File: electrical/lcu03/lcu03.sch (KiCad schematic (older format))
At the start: 93 parts, among them P1 screw, P10 swd, P11 stepper_conn, P12 stepper_conn, P13 stepper_conn, P2 screw, P3 screw, P4 screw, P5 ext-1, P6 ~rst~, P7 mode, P8 ext-2, P9 USB_B, Q1 bc857, Q2 bv847, Q3 bc857, Q4 ntd18n06l, U1 crystal-4pin, U2 CP2102, U3 m24c02, U4 NCP3063, U5 MCP1703T-3302E/CB, U6 ts881, U7 lb1930mc

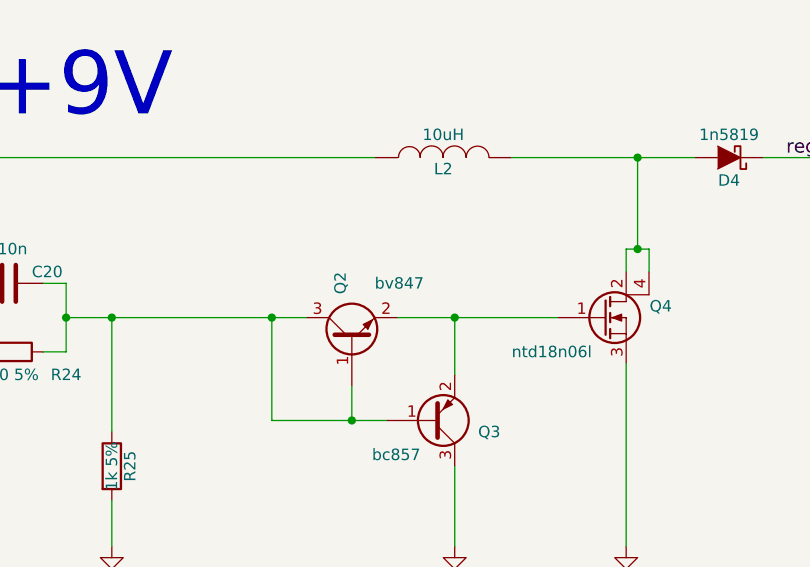
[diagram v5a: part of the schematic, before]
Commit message: Looks like done with assigning footprints.
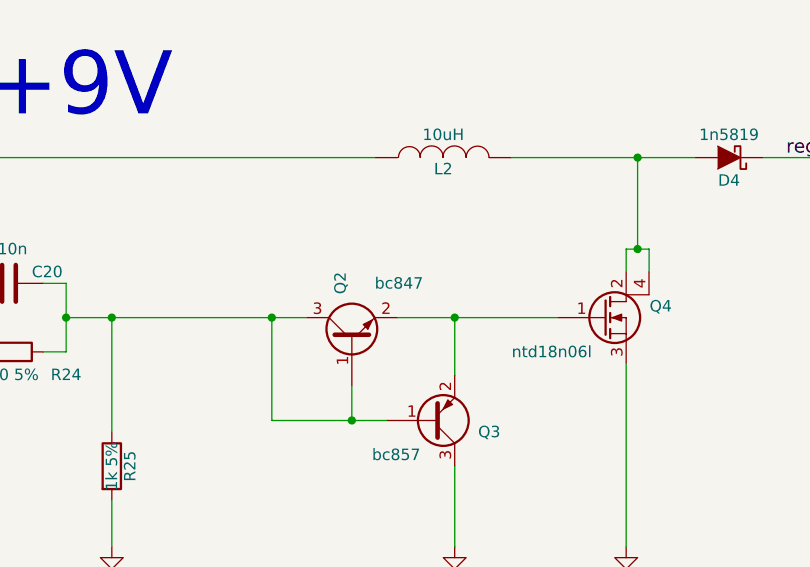
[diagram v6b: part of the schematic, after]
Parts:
- C1, C10, C11, C12, C13, C14, C15, C16, C18, C19, C2, C20, C21, C23, C24, C3, C4, C5, C6, C7, C8, C9: footprint Capacitors_SMD:C_0805_HandSoldering -> Capacitors_SMD:C_0805
- P10: footprint Socket_Strips:Socket_Strip_Straight_1x03 -> Pin_Headers:Pin_Header_Straight_1x03
- P6: footprint Pin_Headers:Pin_Header_Straight_1x01 -> Measurement_Points:Measurement_Point_Round-TH_Small
- P7: footprint Pin_Headers:Pin_Header_Angled_1x02 -> Pin_Headers:Pin_Header_Straight_1x02
- P8: footprint Pin_Headers:Pin_Header_Angled_1x08 -> Pin_Headers:Pin_Header_Straight_1x08
- Q2: value bv847 -> bc847
- Q4: footprint (none) -> my-lib:my-DPAK
- R1, R2, R3, R4, R5, R6, R7, R8: footprint Resistors_SMD:R_0805_HandSoldering -> Resistors_SMD:R_0805
- U7: footprint (none) -> my-lib:lb1930mc
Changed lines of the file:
@@
 F 0 "R8" V 4280 3300 50  0000 C CNN
 F 1 "10k 5%" V 4100 3300 50  0000 C CNN
-F 2 "Resistors_SMD:R_0805_HandSoldering" V 4130 3300 30  0001 C CNN
+F 2 "Resistors_SMD:R_0805" V 4130 3300 30  0001 C CNN
 F 3 "" H 4200 3300 30  0000 C CNN
 	1    4200 3300
@@
 F 0 "C4" H 4225 3800 50  0000 L CNN
 F 1 "100n" H 4225 3600 50  0000 L CNN
-F 2 "Capacitors_SMD:C_0805_HandSoldering" H 4238 3550 30  0001 C CNN
+F 2 "Capacitors_SMD:C_0805" H 4238 3550 30  0001 C CNN
 F 3 "" H 4200 3700 60  0000 C CNN
 	1    4200 3700
@@
 F 0 "C2" H 1675 4150 50  0000 L CNN
 F 1 "18p" H 1675 3950 50  0000 L CNN
-F 2 "Capacitors_SMD:C_0805_HandSoldering" H 1688 3900 30  0001 C CNN
+F 2 "Capacitors_SMD:C_0805" H 1688 3900 30  0001 C CNN
 F 3 "" H 1650 4050 60  0000 C CNN
 	1    1650 4050
@@
 F 0 "C3" H 3375 5350 50  0000 L CNN
 F 1 "18p" H 3375 5150 50  0000 L CNN
-F 2 "Capacitors_SMD:C_0805_HandSoldering" H 3388 5100 30  0001 C CNN
+F 2 "Capacitors_SMD:C_0805" H 3388 5100 30  0001 C CNN
 F 3 "" H 3350 5250 60  0000 C CNN
 	1    3350 5250
@@
 F 0 "R6" V 3830 5000 50  0000 C CNN
 F 1 "100 5%" V 3650 5000 50  0000 C CNN
-F 2 "Resistors_SMD:R_0805_HandSoldering" V 3680 5000 30  0001 C CNN
+F 2 "Resistors_SMD:R_0805" V 3680 5000 30  0001 C CNN
 F 3 "" H 3750 5000 30  0000 C CNN
 	1    3750 5000
@@
 F 0 "R5" V 3780 7950 50  0000 C CNN
 F 1 "10k 5%" V 3700 7950 50  0000 C CNN
-F 2 "Resistors_SMD:R_0805_HandSoldering" V 3630 7950 30  0001 C CNN
+F 2 "Resistors_SMD:R_0805" V 3630 7950 30  0001 C CNN
 F 3 "" H 3700 7950 30  0000 C CNN
 	1    3700 7950
@@
 F 0 "C21" H 16075 17650 50  0000 L CNN
 F 1 "4u7" H 16075 17450 50  0000 L CNN
-F 2 "Capacitors_SMD:C_0805_HandSoldering" H 16088 17400 30  0001 C CNN
+F 2 "Capacitors_SMD:C_0805" H 16088 17400 30  0001 C CNN
 F 3 "" H 16050 17550 60  0000 C CNN
 	1    16050 17550
@@
 F 0 "C18" H 14575 17650 50  0000 L CNN
 F 1 "4u7" H 14575 17450 50  0000 L CNN
-F 2 "Capacitors_SMD:C_0805_HandSoldering" H 14588 17400 30  0001 C CNN
+F 2 "Capacitors_SMD:C_0805" H 14588 17400 30  0001 C CNN
 F 3 "" H 14550 17550 60  0000 C CNN
 	1    14550 17550
@@
 F 0 "C1" H 775 19500 50  0000 L CNN
 F 1 "100n" H 775 19300 50  0000 L CNN
-F 2 "Capacitors_SMD:C_0805_HandSoldering" H 788 19250 30  0001 C CNN
+F 2 "Capacitors_SMD:C_0805" H 788 19250 30  0001 C CNN
 F 3 "" H 750 19400 60  0000 C CNN
 	1    750  19400
@@
 F 0 "R1" V 830 18700 50  0000 C CNN
 F 1 "10k 5%" V 650 18700 50  0000 C CNN
-F 2 "Resistors_SMD:R_0805_HandSoldering" V 680 18700 30  0001 C CNN
+F 2 "Resistors_SMD:R_0805" V 680 18700 30  0001 C CNN
 F 3 "" H 750 18700 30  0000 C CNN
 	1    750  18700
@@
 F 0 "C5" H 5575 19550 50  0000 L CNN
 F 1 "100n" H 5575 19350 50  0000 L CNN
-F 2 "Capacitors_SMD:C_0805_HandSoldering" H 5588 19300 30  0001 C CNN
+F 2 "Capacitors_SMD:C_0805" H 5588 19300 30  0001 C CNN
 F 3 "" H 5550 19450 60  0000 C CNN
 	1    5550 19450
@@
 F 0 "C6" H 5925 19550 50  0000 L CNN
 F 1 "4u7" H 5925 19350 50  0000 L CNN
-F 2 "Capacitors_SMD:C_0805_HandSoldering" H 5938 19300 30  0001 C CNN
+F 2 "Capacitors_SMD:C_0805" H 5938 19300 30  0001 C CNN
 F 3 "" H 5900 19450 60  0000 C CNN
 	1    5900 19450
@@
 F 0 "C15" H 12625 20650 50  0000 L CNN
 F 1 "100n" H 12625 20450 50  0000 L CNN
-F 2 "Capacitors_SMD:C_0805_HandSoldering" H 12638 20400 30  0001 C CNN
+F 2 "Capacitors_SMD:C_0805" H 12638 20400 30  0001 C CNN
 F 3 "" H 12600 20550 60  0000 C CNN
 	1    12600 20550
@@
 F 0 "C19" H 14975 20600 50  0000 L CNN
 F 1 "1n2" H 14975 20400 50  0000 L CNN
-F 2 "Capacitors_SMD:C_0805_HandSoldering" H 14988 20350 30  0001 C CNN
+F 2 "Capacitors_SMD:C_0805" H 14988 20350 30  0001 C CNN
 F 3 "" H 14950 20500 60  0000 C CNN
 	1    14950 20500
@@
 F 0 "C24" H 19225 20050 50  0000 L CNN
 F 1 "100n" H 19225 19850 50  0000 L CNN
-F 2 "Capacitors_SMD:C_0805_HandSoldering" H 19238 19800 30  0001 C CNN
+F 2 "Capacitors_SMD:C_0805" H 19238 19800 30  0001 C CNN
 F 3 "" H 19200 19950 60  0000 C CNN
 	1    19200 19950
@@
 F 0 "R2" V 1280 12600 50  0000 C CNN
 F 1 "1k 5%" V 1200 12600 50  0000 C CNN
-F 2 "Resistors_SMD:R_0805_HandSoldering" V 1130 12600 30  0001 C CNN
+F 2 "Resistors_SMD:R_0805" V 1130 12600 30  0001 C CNN
 F 3 "" H 1200 12600 30  0000 C CNN
 	1    1200 12600
@@
 F 0 "R3" V 1780 12600 50  0000 C CNN
 F 1 "1k 5%" V 1700 12600 50  0000 C CNN
-F 2 "Resistors_SMD:R_0805_HandSoldering" V 1630 12600 30  0001 C CNN
+F 2 "Resistors_SMD:R_0805" V 1630 12600 30  0001 C CNN
 F 3 "" H 1700 12600 30  0000 C CNN
 	1    1700 12600
@@
 F 0 "P7" H 3300 7300 50  0000 C CNN
 F 1 "mode" V 3400 7150 50  0000 C CNN
-F 2 "Pin_Headers:Pin_Header_Angled_1x02" H 3300 7150 60  0001 C CNN
+F 2 "Pin_Headers:Pin_Header_Straight_1x02" H 3300 7150 60  0001 C CNN
 F 3 "" H 3300 7150 60  0000 C CNN
 	1    3300 7150
@@
 F 0 "P10" H 10550 5900 50  0000 C CNN
 F 1 "swd" V 10650 5700 50  0000 C CNN
-F 2 "Socket_Strips:Socket_Strip_Straight_1x03" H 10550 5700 60  0001 C CNN
+F 2 "Pin_Headers:Pin_Header_Straight_1x03" H 10550 5700 60  0001 C CNN
 F 3 "" H 10550 5700 60  0000 C CNN
 	1    10550 5700
@@
 F 0 "P6" H 3250 3600 50  0000 C CNN
 F 1 "~rst~" V 3350 3500 50  0000 C CNN
-F 2 "Pin_Headers:Pin_Header_Straight_1x01" H 3250 3500 60  0001 C CNN
+F 2 "Measurement_Points:Measurement_Point_Round-TH_Small" H 3250 3500 60  0001 C CNN
 F 3 "" H 3250 3500 60  0000 C CNN
 	1    3250 3500
@@
 F 0 "R4" V 3630 12350 50  0000 C CNN
 F 1 "10k 5%" V 3550 12350 50  0000 C CNN
-F 2 "Resistors_SMD:R_0805_HandSoldering" V 3480 12350 30  0001 C CNN
+F 2 "Resistors_SMD:R_0805" V 3480 12350 30  0001 C CNN
 F 3 "" H 3550 12350 30  0000 C CNN
 	1    3550 12350
@@
 F 0 "C8" H 10625 1350 50  0000 L CNN
 F 1 "100n" H 10625 1150 50  0000 L CNN
-F 2 "Capacitors_SMD:C_0805_HandSoldering" H 10638 1100 30  0001 C CNN
+F 2 "Capacitors_SMD:C_0805" H 10638 1100 30  0001 C CNN
 F 3 "" H 10600 1250 60  0000 C CNN
 	1    10600 1250
@@
 F 0 "C9" H 10925 1350 50  0000 L CNN
 F 1 "100n" H 10925 1150 50  0000 L CNN
-F 2 "Capacitors_SMD:C_0805_HandSoldering" H 10938 1100 30  0001 C CNN
+F 2 "Capacitors_SMD:C_0805" H 10938 1100 30  0001 C CNN
 F 3 "" H 10900 1250 60  0000 C CNN
 	1    10900 1250
@@
 F 0 "C10" H 11225 1350 50  0000 L CNN
 F 1 "100n" H 11225 1150 50  0000 L CNN
-F 2 "Capacitors_SMD:C_0805_HandSoldering" H 11238 1100 30  0001 C CNN
+F 2 "Capacitors_SMD:C_0805" H 11238 1100 30  0001 C CNN
 F 3 "" H 11200 1250 60  0000 C CNN
 	1    11200 1250
@@
 F 0 "C11" H 11525 1350 50  0000 L CNN
 F 1 "100n" H 11525 1150 50  0000 L CNN
-F 2 "Capacitors_SMD:C_0805_HandSoldering" H 11538 1100 30  0001 C CNN
+F 2 "Capacitors_SMD:C_0805" H 11538 1100 30  0001 C CNN
 F 3 "" H 11500 1250 60  0000 C CNN
 	1    11500 1250
@@
 F 0 "C12" H 11825 1350 50  0000 L CNN
 F 1 "4u7" H 11825 1150 50  0000 L CNN
-F 2 "Capacitors_SMD:C_0805_HandSoldering" H 11838 1100 30  0001 C CNN
+F 2 "Capacitors_SMD:C_0805" H 11838 1100 30  0001 C CNN
 F 3 "" H 11800 1250 60  0000 C CNN
 	1    11800 1250
@@
 F 0 "R7" V 4230 7950 50  0000 C CNN
 F 1 "10k 5%" V 4150 7950 50  0000 C CNN
-F 2 "Resistors_SMD:R_0805_HandSoldering" V 4080 7950 30  0001 C CNN
+F 2 "Resistors_SMD:R_0805" V 4080 7950 30  0001 C CNN
 F 3 "" H 4150 7950 30  0000 C CNN
 	1    4150 7950
@@
 F 0 "C16" H 13775 20950 50  0000 L CNN
 F 1 "10n" H 13775 20750 50  0000 L CNN
-F 2 "Capacitors_SMD:C_0805_HandSoldering" H 13788 20700 30  0001 C CNN
+F 2 "Capacitors_SMD:C_0805" H 13788 20700 30  0001 C CNN
 F 3 "" H 13750 20850 60  0000 C CNN
 	1    13750 20850
@@
 F 0 "C13" H 12325 20650 50  0000 L CNN
 F 1 "4u7" H 12325 20450 50  0000 L CNN
-F 2 "Capacitors_SMD:C_0805_HandSoldering" H 12338 20400 30  0001 C CNN
+F 2 "Capacitors_SMD:C_0805" H 12338 20400 30  0001 C CNN
 F 3 "" H 12300 20550 60  0000 C CNN
 	1    12300 20550
@@
 F 0 "C20" V 15450 20050 50  0000 L CNN
 F 1 "10n" V 15350 19900 50  0000 L CNN
-F 2 "Capacitors_SMD:C_0805_HandSoldering" H 15538 19800 30  0001 C CNN
+F 2 "Capacitors_SMD:C_0805" H 15538 19800 30  0001 C CNN
 F 3 "" H 15500 19950 60  0000 C CNN
 	1    15500 19950
@@
 P 17000 20200
 F 0 "Q2" H 17300 20250 50  0000 R CNN
-F 1 "bv847" V 17250 20100 50  0000 R CNN
+F 1 "bc847" V 17250 20100 50  0000 R CNN
 F 2 "TO_SOT_Packages_SMD:SOT-23_Handsoldering" H 17200 20300 50  0001 C CNN
 F 3 "" H 17000 20200 50  0000 C CNN
@@
 F 0 "Q4" H 18400 20150 50  0000 R CNN
 F 1 "ntd18n06l" H 18050 19950 50  0000 R CNN
-F 2 "" H 18300 20200 50  0001 C CNN
+F 2 "my-lib:my-DPAK" H 18300 20200 50  0001 C CNN
 F 3 "" H 18100 20100 50  0000 C CNN
 	1    18100 20100
@@
 F 0 "U7" H 21600 1400 60  0000 C CNN
 F 1 "lb1930mc" H 21600 2400 60  0000 C CNN
-F 2 "" H 21600 1900 60  0001 C CNN
+F 2 "my-lib:lb1930mc" H 21600 1900 60  0001 C CNN
 F 3 "" H 21600 1900 60  0000 C CNN
 	1    21600 1900
@@
 F 0 "C14" H 12375 12200 50  0000 L CNN
 F 1 "100n" H 12375 12000 50  0000 L CNN
-F 2 "Capacitors_SMD:C_0805_HandSoldering" H 12388 11950 50  0001 C CNN
+F 2 "Capacitors_SMD:C_0805" H 12388 11950 50  0001 C CNN
 F 3 "" H 12350 12100 50  0000 C CNN
 	1    12350 12100
@@
 F 0 "C7" H 6075 22100 50  0000 L CNN
 F 1 "4u7" H 6075 21900 50  0000 L CNN
-F 2 "Capacitors_SMD:C_0805_HandSoldering" H 6088 21850 30  0001 C CNN
+F 2 "Capacitors_SMD:C_0805" H 6088 21850 30  0001 C CNN
 F 3 "" H 6050 22000 60  0000 C CNN
 	1    6050 22000
@@
 F 0 "C23" H 17825 9050 50  0000 L CNN
 F 1 "100n" H 17825 8850 50  0000 L CNN
-F 2 "Capacitors_SMD:C_0805_HandSoldering" H 17838 8800 50  0001 C CNN
+F 2 "Capacitors_SMD:C_0805" H 17838 8800 50  0001 C CNN
 F 3 "" H 17800 8950 50  0000 C CNN
 	1    17800 8950
@@
 F 0 "P8" H 4550 13350 50  0000 C CNN
 F 1 "ext-2" V 4650 12900 50  0000 C CNN
-F 2 "Pin_Headers:Pin_Header_Angled_1x08" H 4550 12900 50  0001 C CNN
+F 2 "Pin_Headers:Pin_Header_Straight_1x08" H 4550 12900 50  0001 C CNN
 F 3 "" H 4550 12900 50  0000 C CNN
 	1    4550 12900

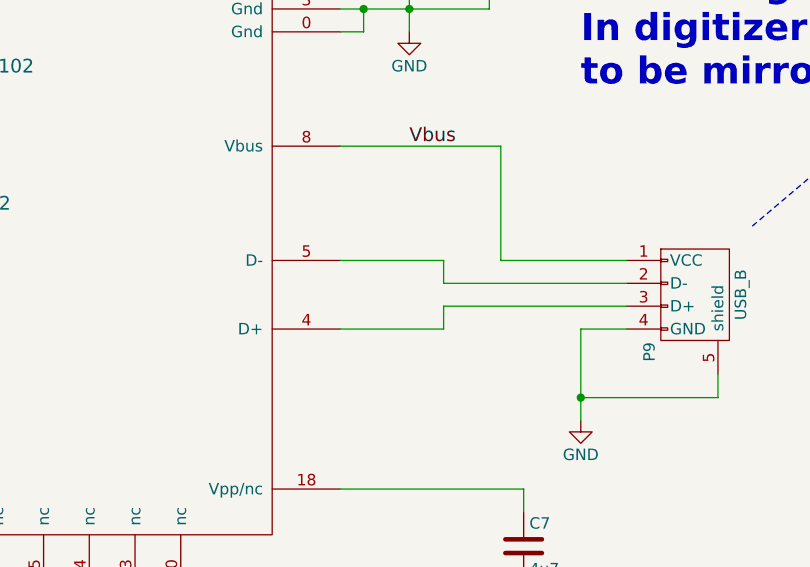
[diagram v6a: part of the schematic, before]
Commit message: Started placing components.
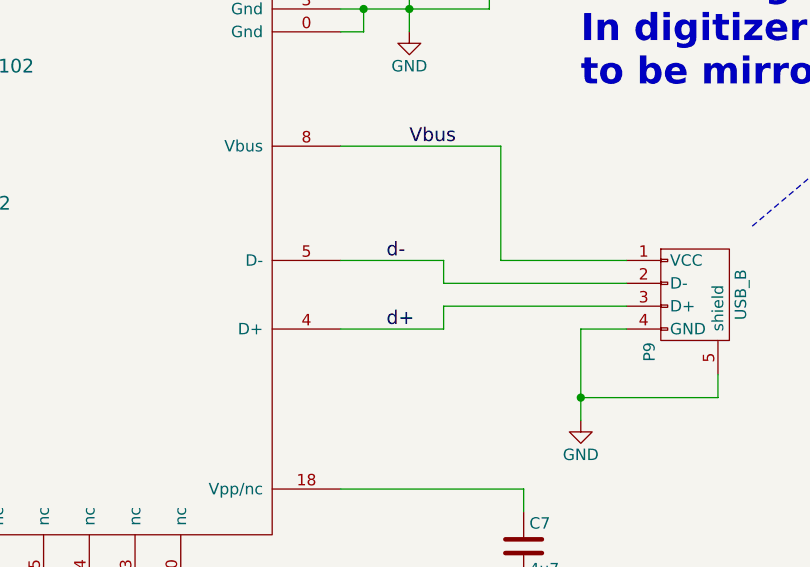
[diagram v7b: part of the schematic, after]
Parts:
- P11, P12, P13: footprint Connectors_JST_PH:Connectors_JST_B4B-PH-SM4-TB -> my-lib:JST_B4B-PH-SM4-TB
- P5: footprint Pin_Headers:Pin_Header_Angled_1x08 -> Pin_Headers:Pin_Header_Straight_1x08
- Q1, Q2, Q3, U5: footprint TO_SOT_Packages_SMD:SOT-23_Handsoldering -> TO_SOT_Packages_SMD:SOT-23
- U1: footprint crystal-smd-5x3:CRYSTAL-SMD-5x3 -> my-lib:CRYSTAL-SMD-5x3
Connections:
- net labels added: d+, d-
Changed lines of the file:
@@
 F 0 "U1" H 2550 4350 60  0000 C CNN
 F 1 "crystal-4pin" H 2550 5000 60  0000 C CNN
-F 2 "crystal-smd-5x3:CRYSTAL-SMD-5x3" H 2500 4650 60  0001 C CNN
+F 2 "my-lib:CRYSTAL-SMD-5x3" H 2500 4650 60  0001 C CNN
 F 3 "" H 2500 4650 60  0000 C CNN
 	1    2550 4650
@@
 F 0 "U5" H 15300 17250 60  0000 C CNN
 F 1 "MCP1703T-3302E/CB" H 15300 17600 60  0000 C CNN
-F 2 "TO_SOT_Packages_SMD:SOT-23_Handsoldering" H 15300 17300 60  0001 C CNN
+F 2 "TO_SOT_Packages_SMD:SOT-23" H 15300 17300 60  0001 C CNN
 F 3 "" H 15300 17300 60  0000 C CNN
 	1    15300 17300
@@
 F 0 "Q2" H 17300 20250 50  0000 R CNN
 F 1 "bc847" V 17250 20100 50  0000 R CNN
-F 2 "TO_SOT_Packages_SMD:SOT-23_Handsoldering" H 17200 20300 50  0001 C CNN
+F 2 "TO_SOT_Packages_SMD:SOT-23" H 17200 20300 50  0001 C CNN
 F 3 "" H 17000 20200 50  0000 C CNN
 	1    17000 20200
@@
 F 0 "Q3" H 17650 20600 50  0000 R CNN
 F 1 "bc857" H 17300 20700 50  0000 R CNN
-F 2 "TO_SOT_Packages_SMD:SOT-23_Handsoldering" H 17550 20650 50  0001 C CNN
+F 2 "TO_SOT_Packages_SMD:SOT-23" H 17550 20650 50  0001 C CNN
 F 3 "" H 17350 20550 50  0000 C CNN
 	1    17350 20550
@@
 F 0 "Q1" H 15700 5000 50  0000 R CNN
 F 1 "bc857" H 15350 5100 50  0000 R CNN
-F 2 "TO_SOT_Packages_SMD:SOT-23_Handsoldering" H 15600 5050 50  0001 C CNN
+F 2 "TO_SOT_Packages_SMD:SOT-23" H 15600 5050 50  0001 C CNN
 F 3 "" H 15400 4950 50  0000 C CNN
 	1    15400 4950
@@
 F 0 "P11" H 24900 2150 50  0000 C CNN
 F 1 "stepper_conn" V 24950 1800 50  0000 C CNN
-F 2 "Connectors_JST_PH:Connectors_JST_B4B-PH-SM4-TB" H 24850 1900 50  0001 C CNN
+F 2 "my-lib:JST_B4B-PH-SM4-TB" H 24850 1900 50  0001 C CNN
 F 3 "" H 24850 1900 50  0000 C CNN
 	1    24850 1900
@@
 F 0 "P12" H 28350 5400 50  0000 C CNN
 F 1 "stepper_conn" V 28400 5050 50  0000 C CNN
-F 2 "Connectors_JST_PH:Connectors_JST_B4B-PH-SM4-TB" H 28300 5150 50  0001 C CNN
+F 2 "my-lib:JST_B4B-PH-SM4-TB" H 28300 5150 50  0001 C CNN
 F 3 "" H 28300 5150 50  0000 C CNN
 	1    28300 5150
@@
 F 0 "P13" H 30650 5400 50  0000 C CNN
 F 1 "stepper_conn" V 30700 5050 50  0000 C CNN
-F 2 "Connectors_JST_PH:Connectors_JST_B4B-PH-SM4-TB" H 30600 5150 50  0001 C CNN
+F 2 "my-lib:JST_B4B-PH-SM4-TB" H 30600 5150 50  0001 C CNN
 F 3 "" H 30600 5150 50  0000 C CNN
 	1    30600 5150
@@
 F 0 "P5" H 2400 13350 50  0000 C CNN
 F 1 "ext-1" V 2500 12900 50  0000 C CNN
-F 2 "Pin_Headers:Pin_Header_Angled_1x08" H 2400 12900 50  0001 C CNN
+F 2 "Pin_Headers:Pin_Header_Straight_1x08" H 2400 12900 50  0001 C CNN
 F 3 "" H 2400 12900 50  0000 C CNN
 	1    2400 12900
@@
 	1    0    0    -1
 $EndComp
+Text Label 5450 20750 0    60   ~ 0
+d-
+Text Label 5450 21050 0    60   ~ 0
+d+
 $EndSCHEMATC

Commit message: a
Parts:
- removed C17: 680u, Capacitors_ThroughHole:C_Radial_D10_L20_P5, symbol CP
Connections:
- wire segments 367 -> 365
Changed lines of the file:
@@
 This diode prevents sucking \nvoltage back from here when \npower is off.
-$Comp
-L CP C17
-U 1 1 566AE216
-P 14300 17550
-F 0 "C17" H 14325 17650 50  0000 L CNN
-F 1 "680u" H 14325 17450 50  0000 L CNN
-F 2 "Capacitors_ThroughHole:C_Radial_D10_L20_P5" H 14338 17400 30  0001 C CNN
-F 3 "" H 14300 17550 60  0000 C CNN
-	1    14300 17550
-	1    0    0    -1
-$EndComp
-Wire Wire Line
-	14300 17400 14300 17200
-Connection ~ 14300 17200
-Wire Wire Line
-	14300 17700 14300 17800
-$Comp
-L GND #PWR049
-U 1 1 566AEB72
-P 14300 17800
-F 0 "#PWR049" H 14300 17550 50  0001 C CNN
-F 1 "GND" H 14300 17650 50  0000 C CNN
-F 2 "" H 14300 17800 60  0000 C CNN
-F 3 "" H 14300 17800 60  0000 C CNN
-	1    14300 17800
-	1    0    0    -1
-$EndComp
 $Comp
 L R R15
